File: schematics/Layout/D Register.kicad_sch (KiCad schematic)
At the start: 4 parts

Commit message: Update layout to KiCad 9.0.1, add adder portion of ALU, add 2 bit adder component.
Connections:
- new net: B11. (OUT4), B13. (OUT8), B14. (OUT8) (x4)
- new net: B12. (OUT4), B13. (OUT8), B14. (OUT8) (x4)

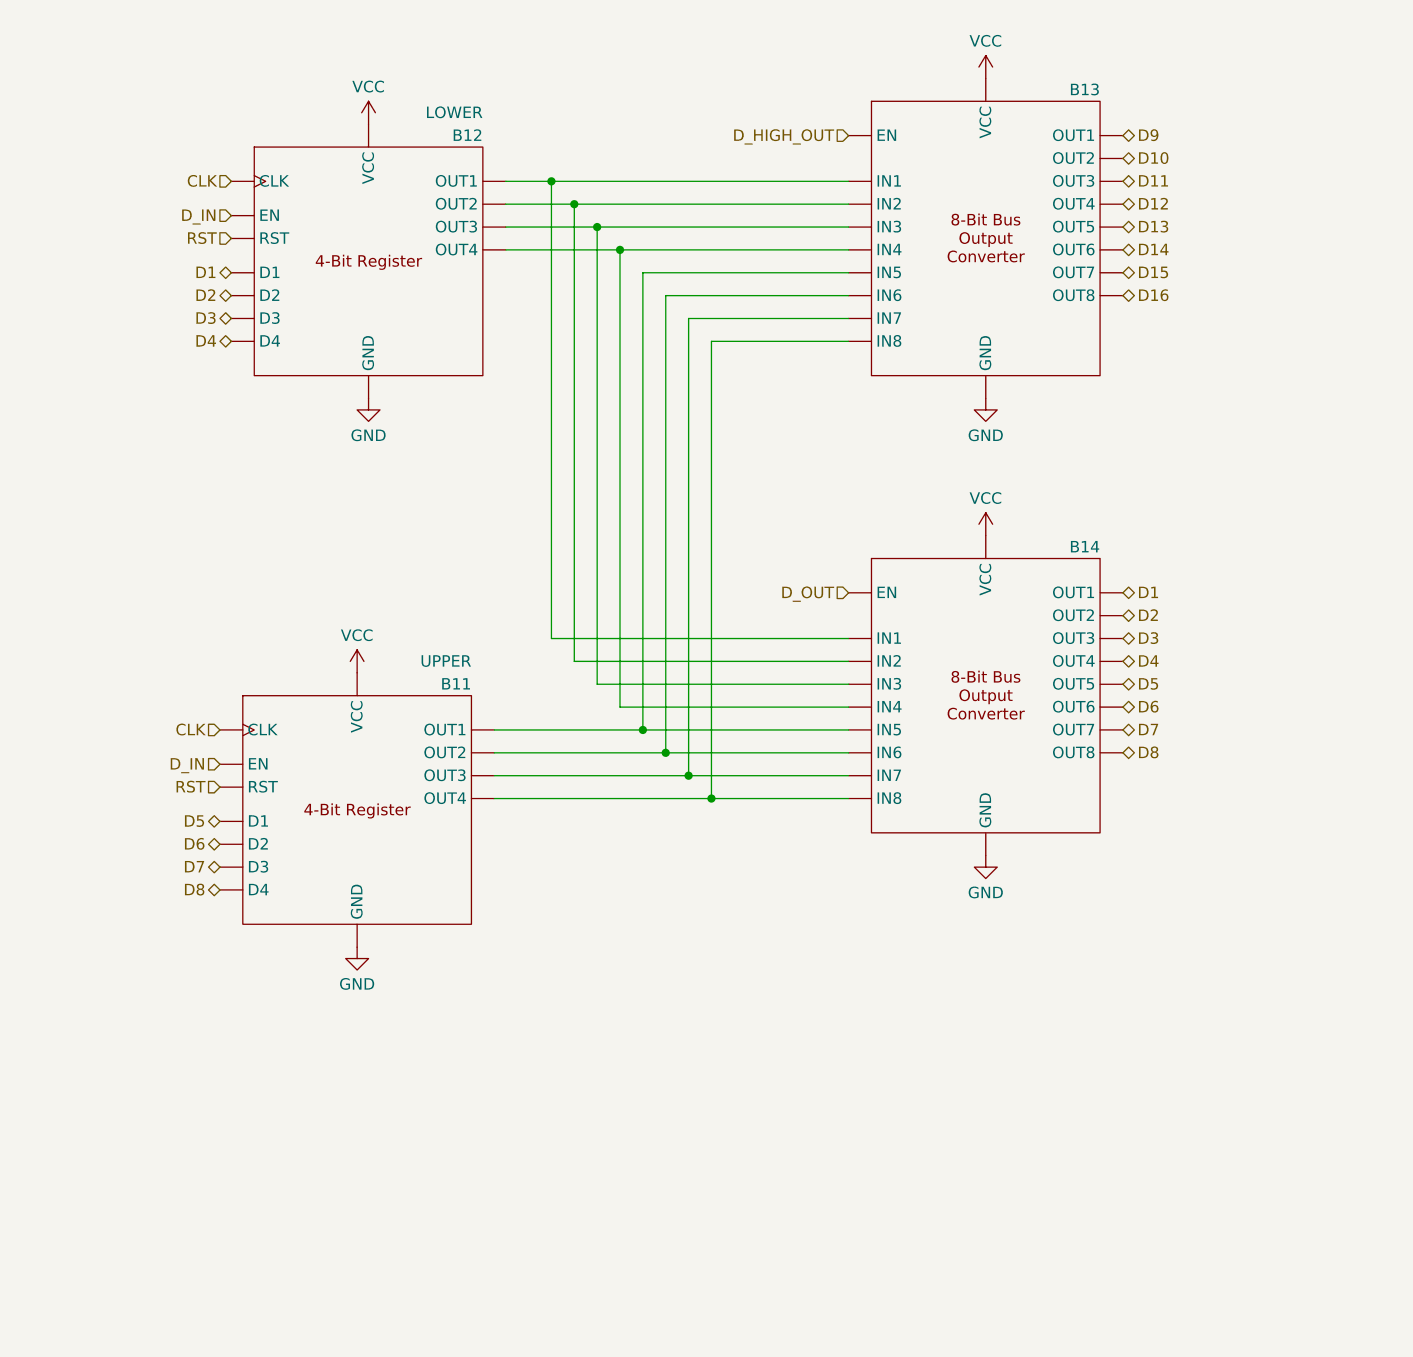
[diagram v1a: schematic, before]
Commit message: Update layout diagram with new boards in following places:  - Added buffer boards to all register boards.  - Fixed PC not getting address lines.  - Added SRAM interface boards.  - Updated to use Mini Control Signals Distributors.
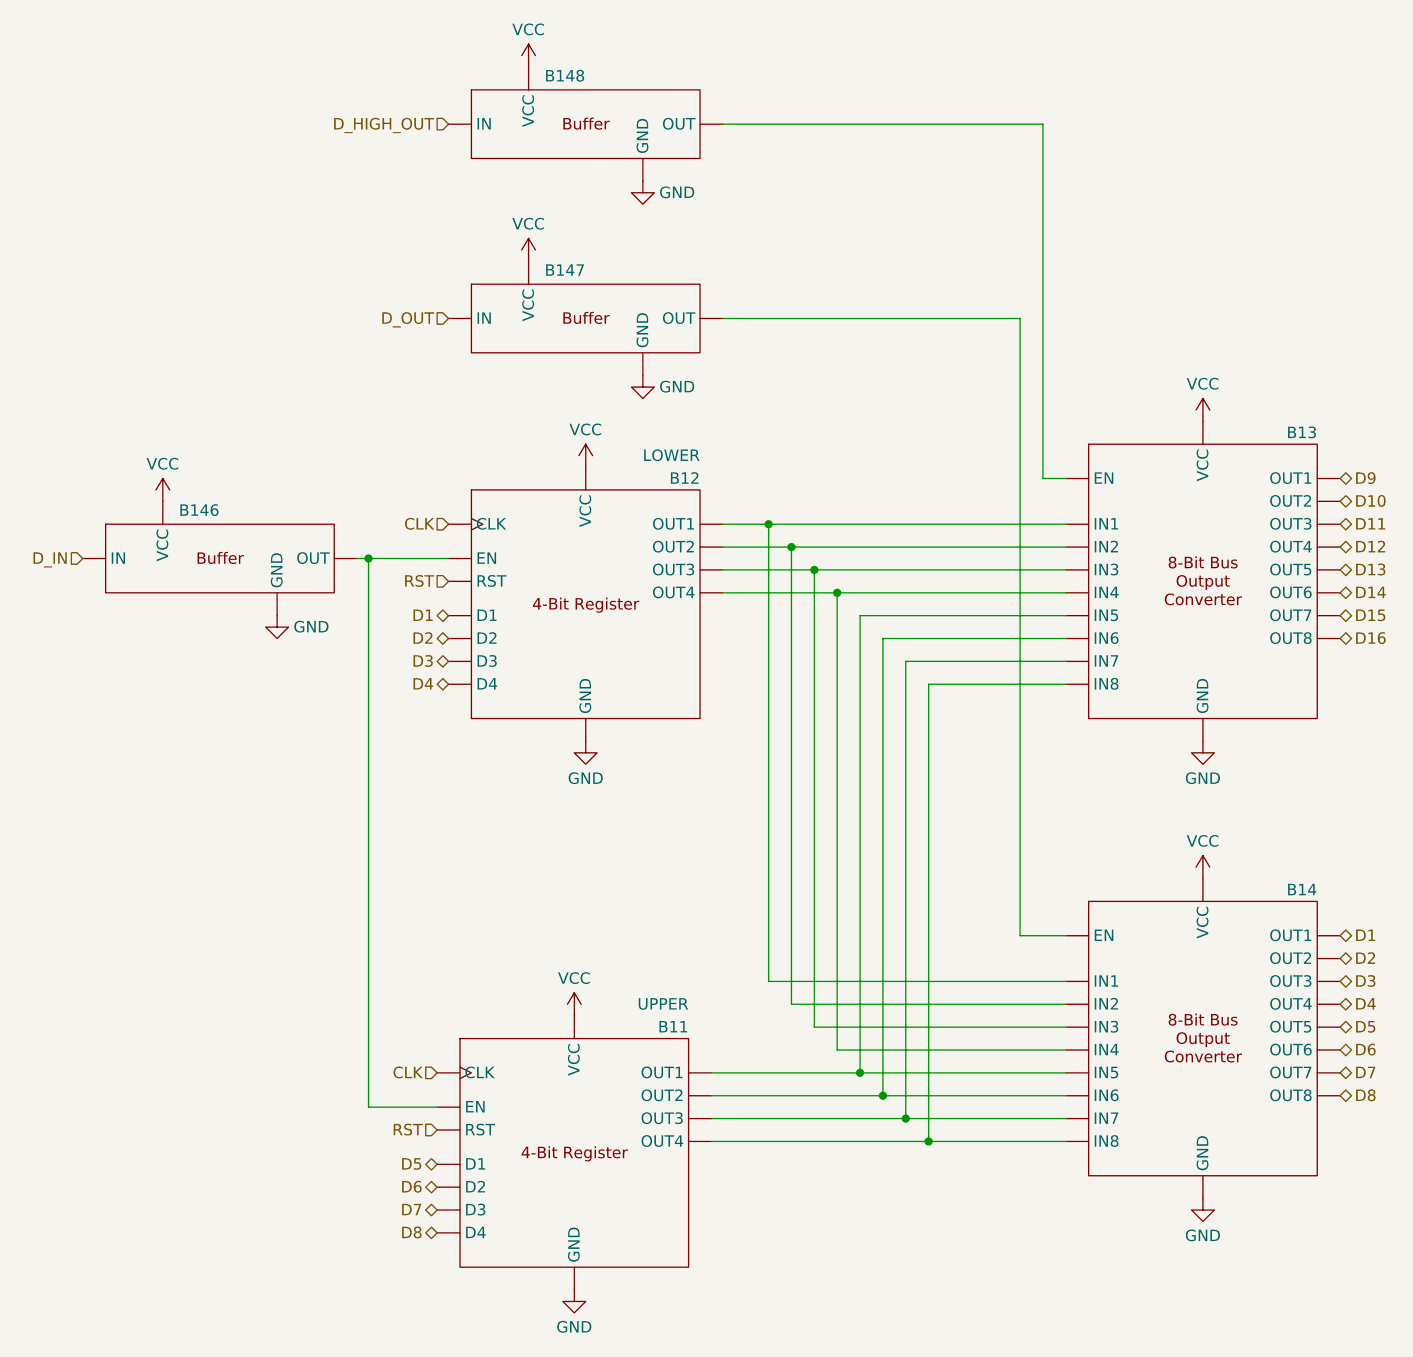
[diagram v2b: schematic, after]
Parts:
- added B146, B147, B148: ~, symbol MiniDragon:Logic Buffer
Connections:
- net D_HIGH_OUT: now also B148. (OUT); no longer B13. (OUT8)
- net D_IN: now also B146. (OUT); no longer B11. (OUT4), B12. (OUT4)
- net D_OUT: now also B147. (OUT); no longer B14. (OUT8)
- net GND: now also B146. (OUT), B147. (OUT), B148. (OUT)
- net VCC: now also B146. (OUT), B147. (OUT), B148. (OUT)
- new net: B11. (OUT4), B13. (OUT8), B14. (OUT8) (x4)
- new net: B11. (OUT4), B12. (OUT4), B146. (OUT)
- new net: B12. (OUT4), B13. (OUT8), B14. (OUT8) (x4)
- new net: B13. (OUT8), B148. (OUT)
- new net: B14. (OUT8), B147. (OUT)
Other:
- moved on the sheet: B11, B12, B13, B14

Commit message: Update with new Shift symbol, diagram the rest of the ALU and more instruction decoder boards.
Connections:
- new net: B11. (OUT4), B13. (OUT8), B14. (OUT8) (x4)
- new net: B11. (OUT4), B12. (OUT4), B146. (OUT)
- new net: B12. (OUT4), B13. (OUT8), B14. (OUT8) (x4)
- new net: B13. (OUT8), B148. (OUT)
- new net: B14. (OUT8), B147. (OUT)
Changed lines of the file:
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@@
 	)
 	(symbol
-		(lib_name "Logic Buffer_1")
+		(lib_name "Logic Buffer_2")
 		(lib_id "MiniDragon:Logic Buffer")
 		(at 100.33 57.15 0)
@@
 	)
 	(symbol
-		(lib_name "Logic Buffer_3")
 		(lib_id "MiniDragon:Logic Buffer")
 		(at 59.69 83.82 0)
@@
 	)
 	(symbol
-		(lib_name "Logic Buffer_2")
+		(lib_name "Logic Buffer_1")
 		(lib_id "MiniDragon:Logic Buffer")
 		(at 100.33 35.56 0)
